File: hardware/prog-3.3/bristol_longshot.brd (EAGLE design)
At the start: 14 x 9 mm, 2 parts

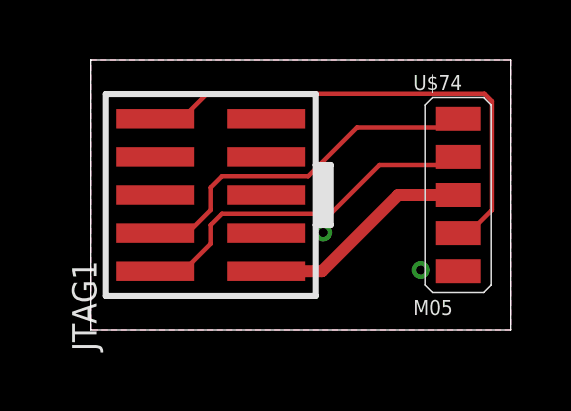
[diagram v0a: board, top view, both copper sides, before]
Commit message: Updated many parts lists, updated bard numbering, removed makefiles for inactive things
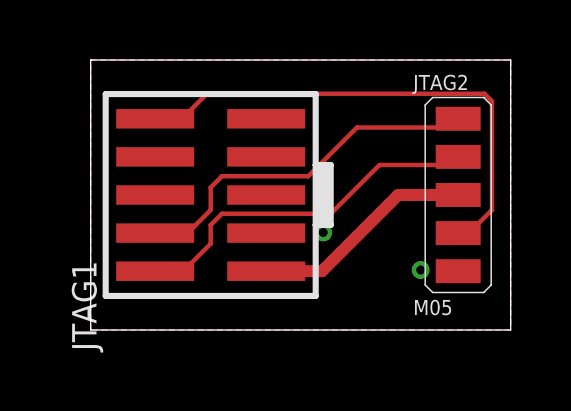
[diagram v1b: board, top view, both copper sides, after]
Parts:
- renumbered U$74 to JTAG2
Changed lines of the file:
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@@
 </autorouter>
 <elements>
-<element name="U$74" library="fbri" package="M05_SIDE" value="M05" x="12.25" y="4.5"/>
+<element name="JTAG2" library="fbri" package="M05_SIDE" value="M05" x="12.25" y="4.5"/>
 <element name="JTAG1" library="microbuilder_v3" package="2X05_1.27MM_SMT" value="" x="4" y="4.5" rot="R90"/>
 </elements>
@@
 <vertex x="0" y="0"/>
 </polygon>
-<contactref element="U$74" pad="$1"/>
+<contactref element="JTAG2" pad="$1"/>
 <contactref element="JTAG1" pad="3"/>
 <contactref element="JTAG1" pad="5"/>
@@
 </signal>
 <signal name="SWDIO">
-<contactref element="U$74" pad="$4"/>
+<contactref element="JTAG2" pad="$4"/>
 <contactref element="JTAG1" pad="2"/>
 <wire x1="2.15" y1="1.96" x2="3.085" y2="1.96" width="0.15" layer="1"/>
@@
 </signal>
 <signal name="SWDCLK">
-<contactref element="U$74" pad="$5"/>
+<contactref element="JTAG2" pad="$5"/>
 <contactref element="JTAG1" pad="4"/>
 <wire x1="2.15" y1="3.23" x2="3.23" y2="3.23" width="0.15" layer="1"/>
@@
 </signal>
 <signal name="EXT!RESET">
-<contactref element="U$74" pad="$2"/>
+<contactref element="JTAG2" pad="$2"/>
 <contactref element="JTAG1" pad="10"/>
 <wire x1="12.25" y1="3.23" x2="12.605" y2="3.23" width="0.15" layer="1"/>
@@
 <signal name="3.3V">
 <contactref element="JTAG1" pad="1"/>
-<contactref element="U$74" pad="$3"/>
+<contactref element="JTAG2" pad="$3"/>
 <wire x1="5.85" y1="1.96" x2="7.71" y2="1.96" width="0.4" layer="1"/>
 <wire x1="7.71" y1="1.96" x2="10.25" y2="4.5" width="0.4" layer="1"/>
